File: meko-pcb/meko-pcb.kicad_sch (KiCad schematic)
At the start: 100 parts, among them IC1 AS5600-ASOM, J1 GDEY0154D67, J2 MEM2090-00-145-00-A, J3 USB_C_Receptacle_USB2.0_16P, M1 HD-EMB1204-SM, Q3 SS8050, Q4 Si1308EDL, SW1 SW_Push, SW2 SW_Push, SW3 SW_Push, SW4 SW_Push, SW5 SW_Push, SW6 SW_Push, SW7 SW_Push, U1 nRF5340-QKxx, U2 nPM1300-QEXX, Y2 32MHz, Y4 32.768 kHz

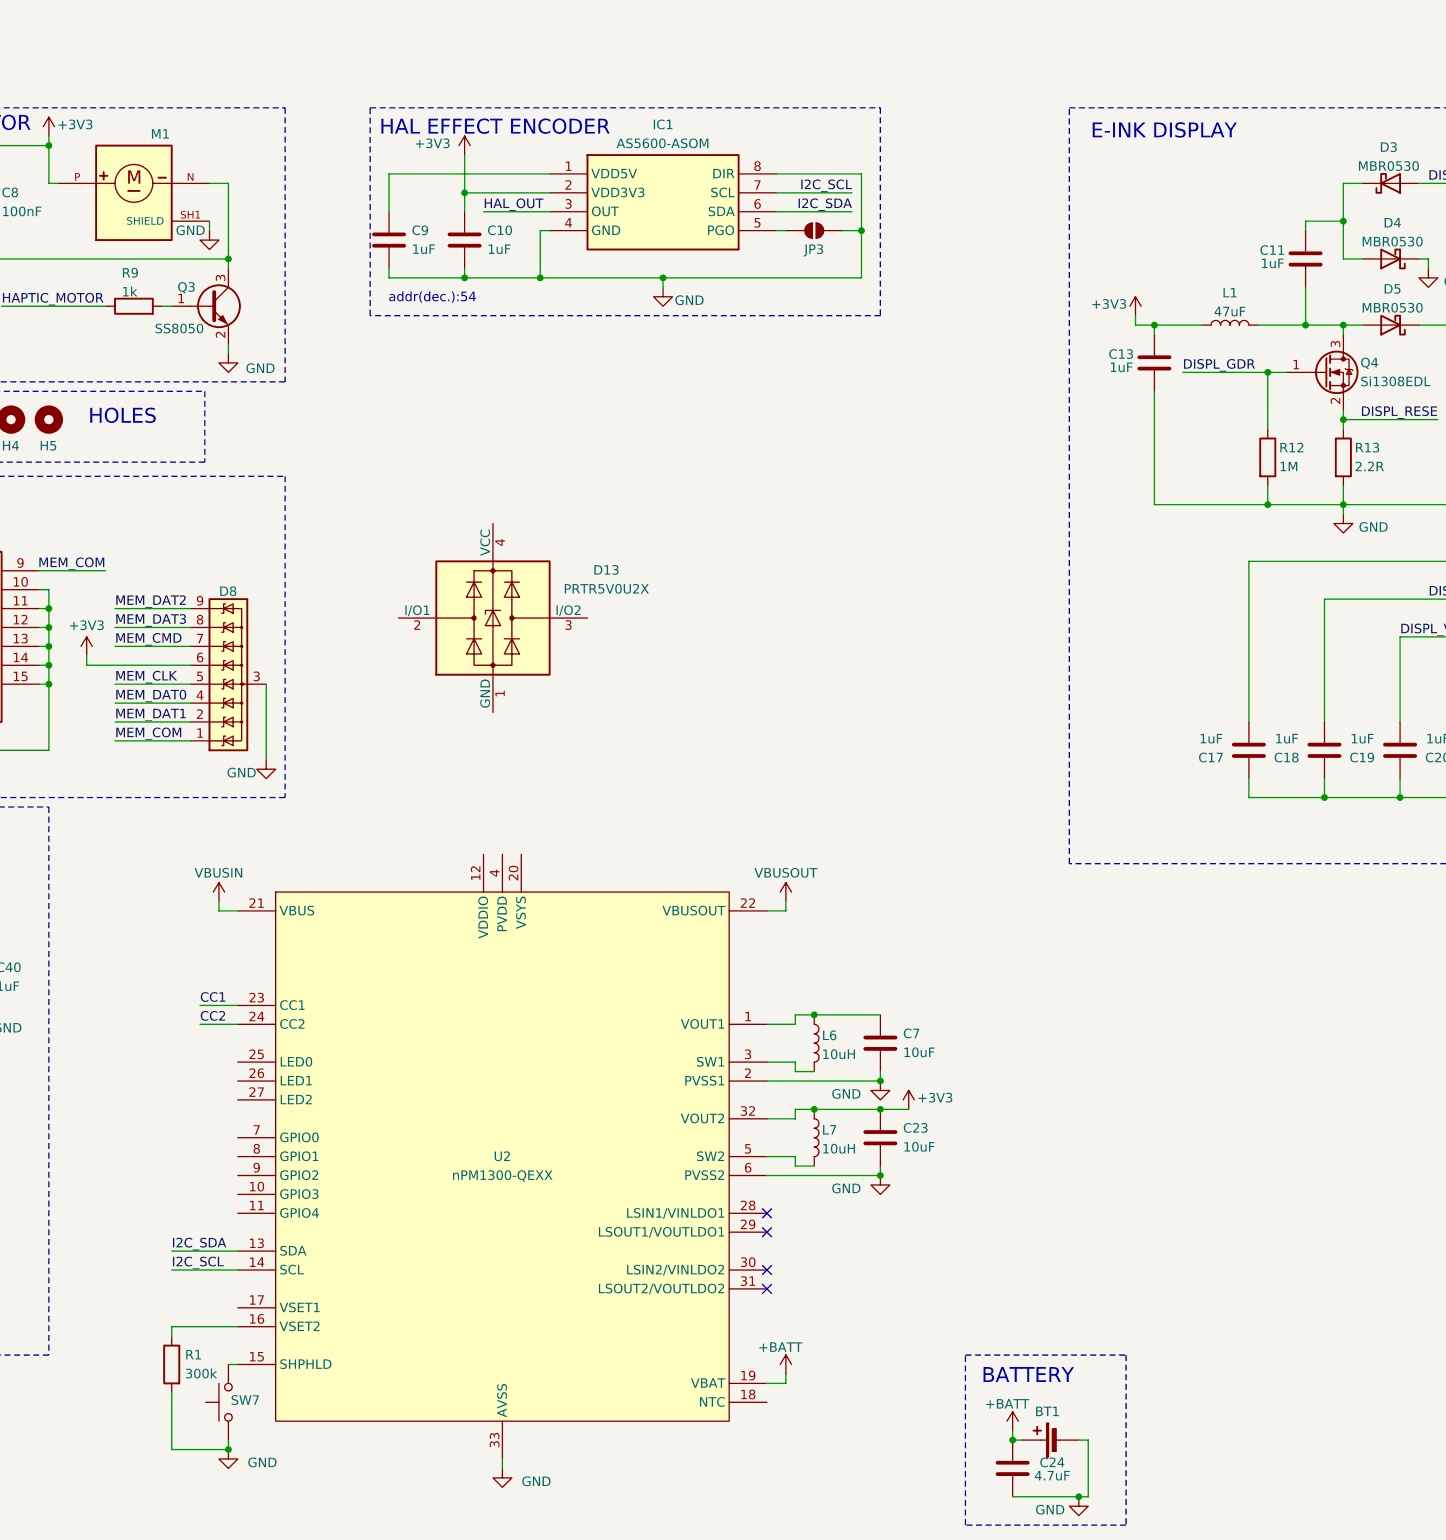
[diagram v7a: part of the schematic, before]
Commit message: added new ldos, made improvements to the schematic
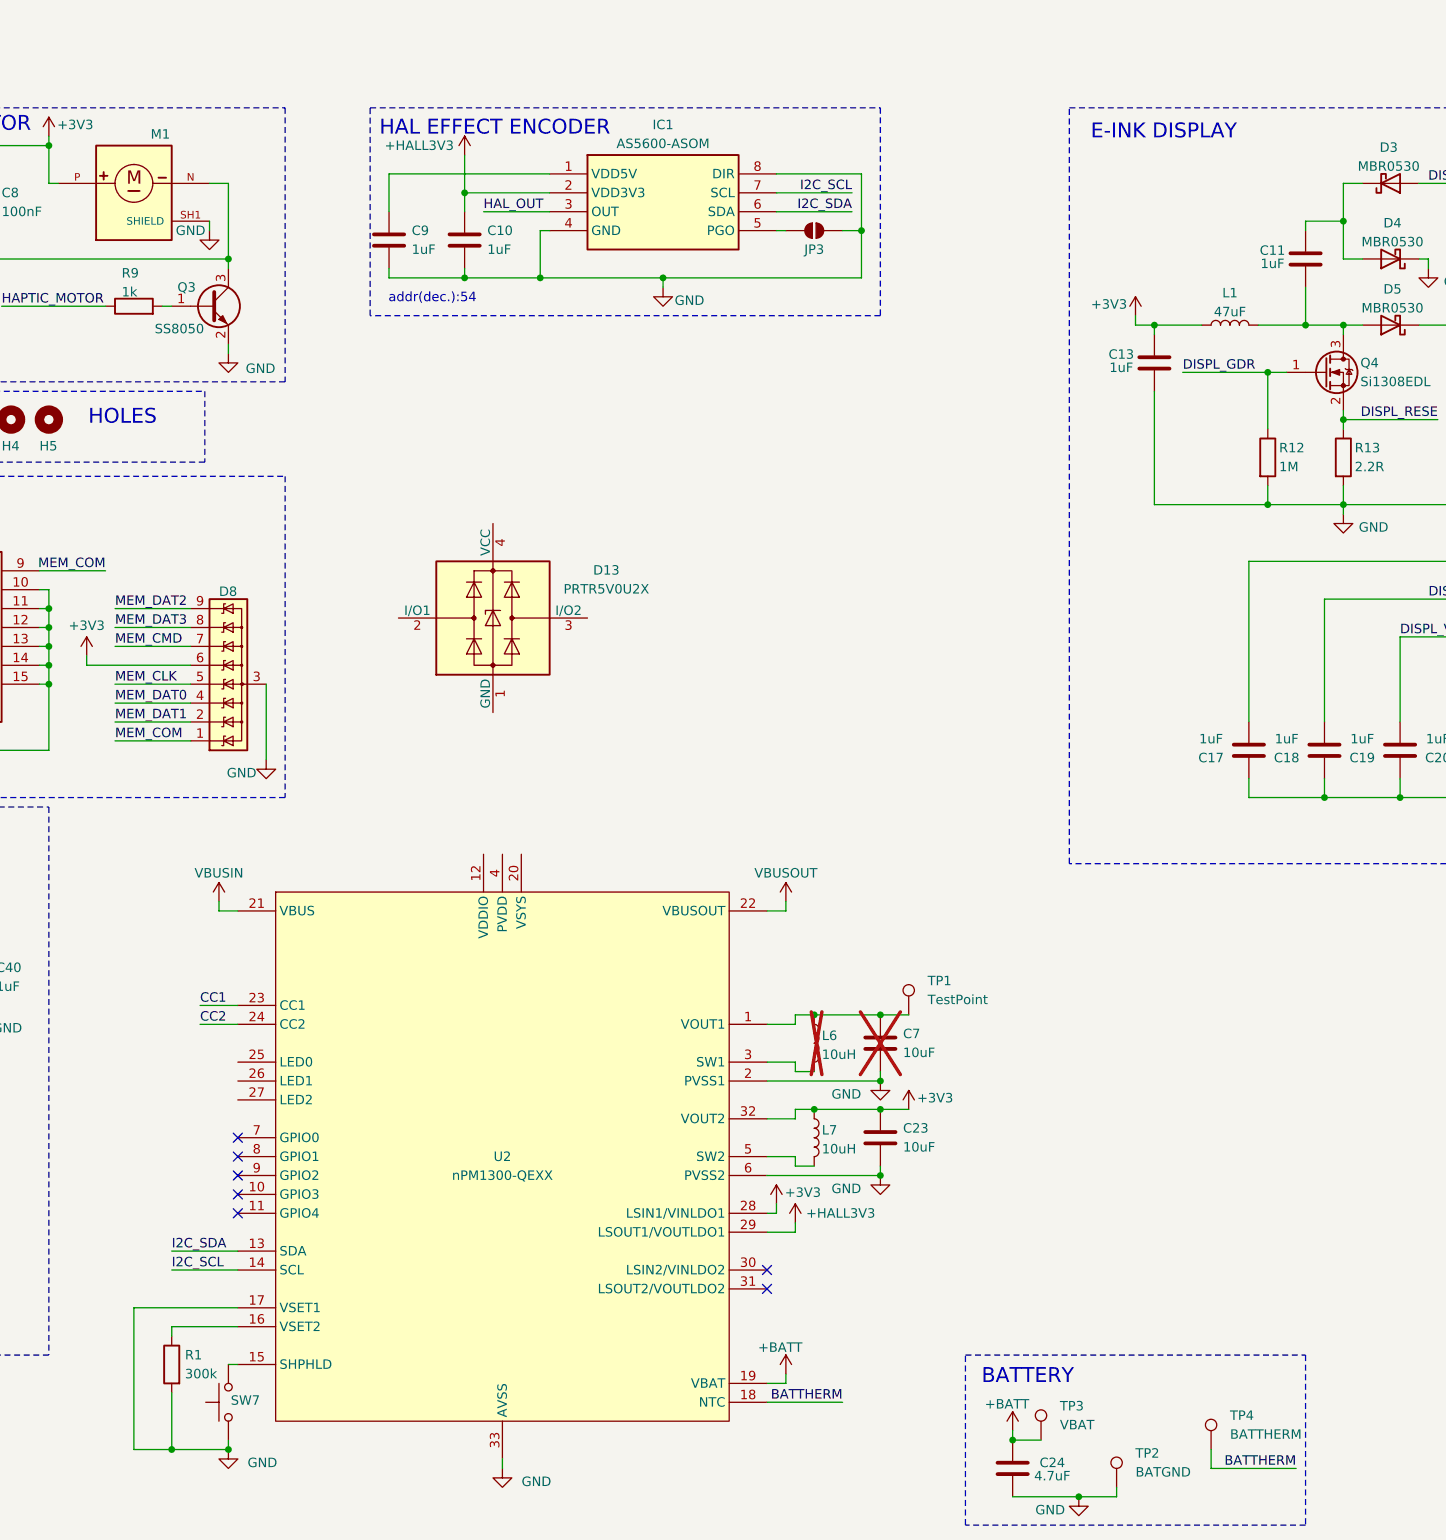
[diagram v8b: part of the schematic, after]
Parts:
- removed BT1: Battery_Cell, S2B-PH-SM4-TB_LF__SN_:JST_S2B-PH-SM4-TB_LF__SN_, symbol Device:Battery_Cell
- added TP1: TestPoint, symbol Connector:TestPoint
- added TP2: BATGND, symbol Connector:TestPoint
- added TP3: VBAT, symbol Connector:TestPoint
- added TP4: BATTHERM, symbol Connector:TestPoint
- C7, L6: now not fitted
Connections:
- net +3V3: now also U2.28 (LSIN1/VINLDO1); no longer C10.1, IC1.2 (VDD3V3)
- net +BATT: now also TP3.1
- net GND: now also U2.17 (VSET1), TP2.1
- net at C7.1, L6.1, U2.1 (VOUT1): now also TP1.1
- net BATTHERM: now reaches U2.18 (NTC)
- net BATTHERM: now also TP4.1
- net +HALL3V3: now reaches U2.29 (LSOUT1/VOUTLDO1)
- net +HALL3V3: now also C10.1, IC1.2 (VDD3V3)
- no-connect marks 12 -> 15
